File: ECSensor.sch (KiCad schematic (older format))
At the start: 11 parts, among them J4 EC_Sensor_Input_3_Pin, Q1 Q_PMOS_DSG

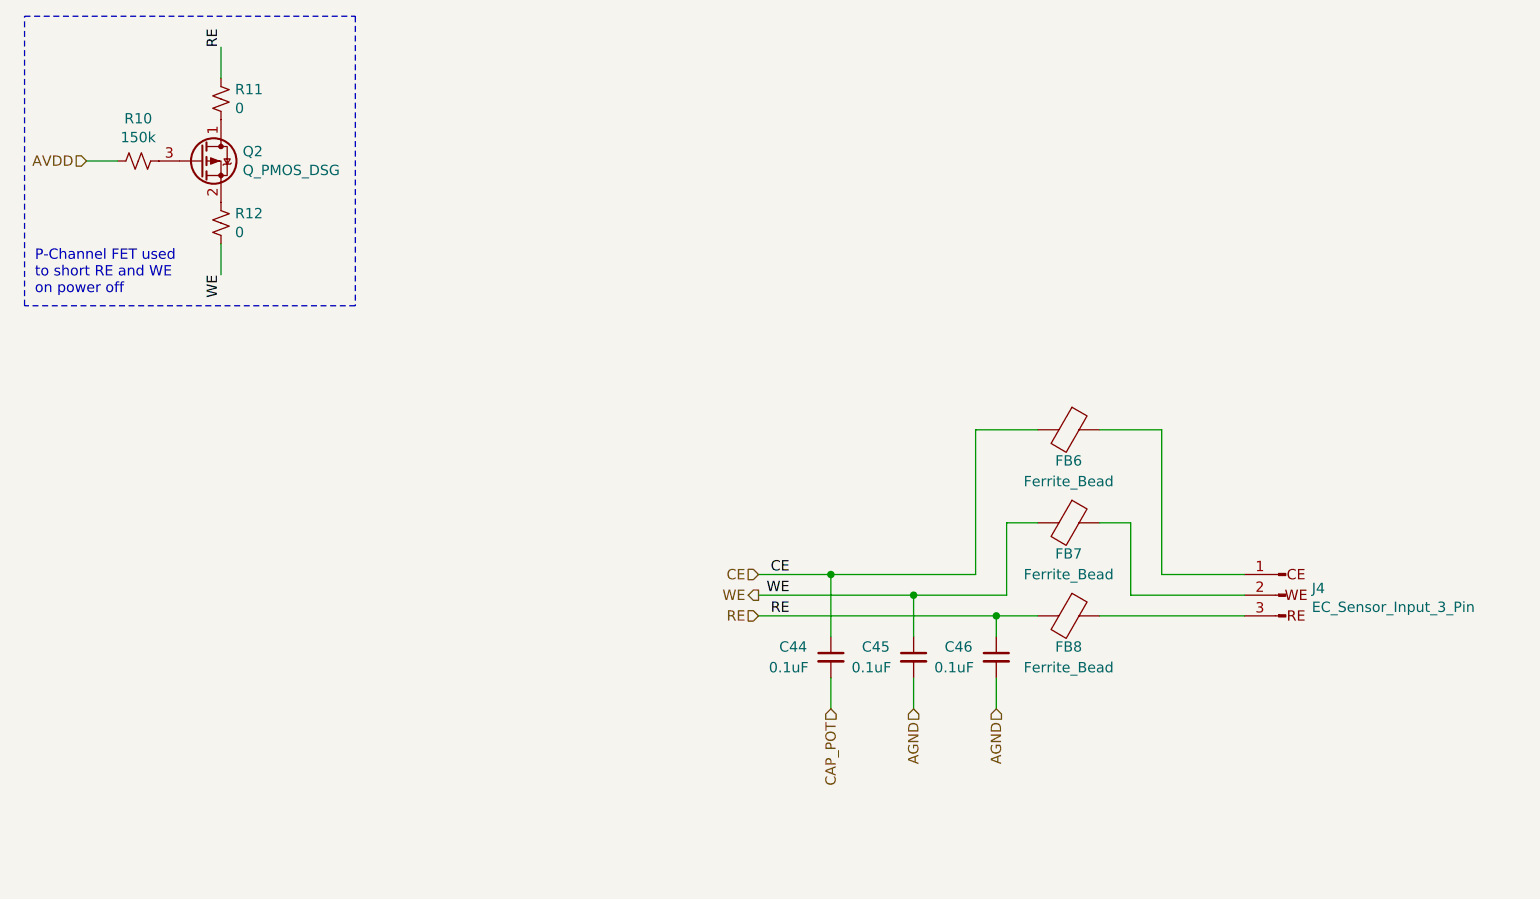
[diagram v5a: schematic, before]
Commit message: removed unneccary components to free up both channels
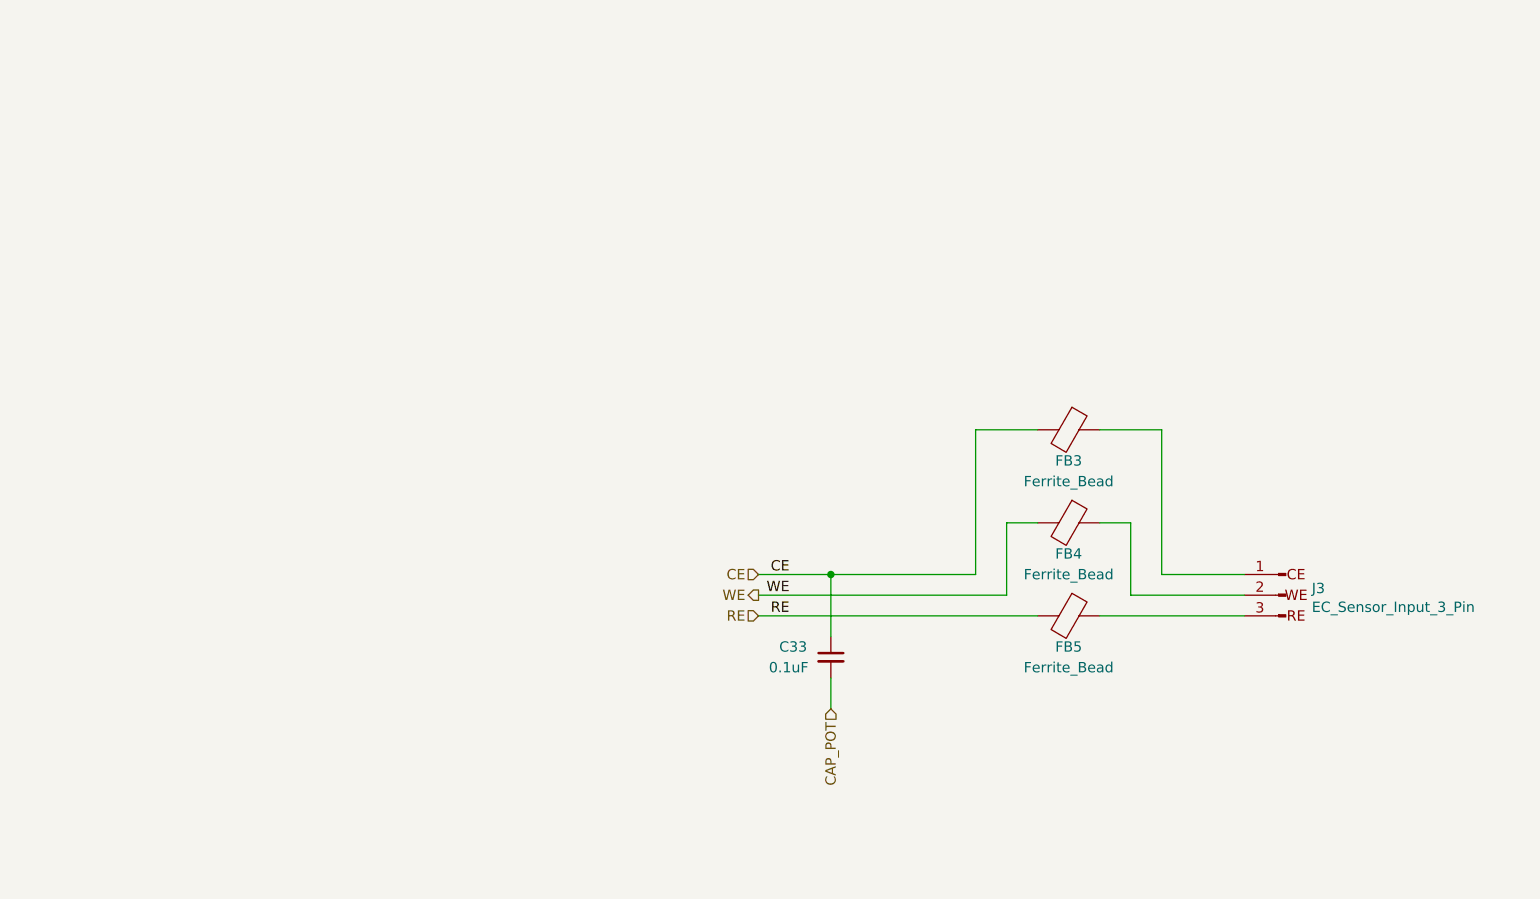
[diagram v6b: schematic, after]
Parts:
- removed C45, C46: 0.1uF, Capacitor_SMD:C_0402_1005Metric, symbol Device:C_Small
- removed Q1: Q_PMOS_DSG, Package_TO_SOT_SMD:SOT-23, symbol Device:Q_PMOS_DSG
- removed R7: 150k, Resistor_SMD:R_0402_1005Metric, symbol Device:R_Small_US
- removed R8, R9: 0, Resistor_SMD:R_0402_1005Metric, symbol Device:R_Small_US
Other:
- note removed: "P-Channel FET used \nto short RE and WE\non power off"
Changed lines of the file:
@@
 $Descr A4 11693 8268
 encoding utf-8
-Sheet 5 5
+Sheet 2 5
 Title "Potentiostat Frontend"
 Date "2021-02-10"
@@
 $EndDescr
 $Comp
-L Device:C_Small C45
-U 1 1 5DF76279
-P 5000 3750
-AR Path="/5DF7340A/5DF76279" Ref="C45"  Part="1"
-AR Path="/5DF54D0C/5DF76279" Ref="C34"  Part="1"
-F 0 "C45" H 4750 3800 50  0000 L CNN
-F 1 "0.1uF" H 4700 3700 50  0000 L CNN
-F 2 "Capacitor_SMD:C_0402_1005Metric" H 5000 3750 50  0001 C CNN
-F 3 "~" H 5000 3750 50  0001 C CNN
-	1    5000 3750
-	1    0    0    -1
-$EndComp
-$Comp
 L Device:C_Small C44
 U 1 1 5DF76497
@@
 AR Path="/5DF7340A/5DF76497" Ref="C44"  Part="1"
 AR Path="/5DF54D0C/5DF76497" Ref="C33"  Part="1"
-F 0 "C44" H 4350 3800 50  0000 L CNN
+F 0 "C33" H 4350 3800 50  0000 L CNN
 F 1 "0.1uF" H 4300 3700 50  0000 L CNN
 F 2 "Capacitor_SMD:C_0402_1005Metric" H 4600 3750 50  0001 C CNN
 F 3 "~" H 4600 3750 50  0001 C CNN
 	1    4600 3750
-	1    0    0    -1
-$EndComp
-$Comp
-L Device:C_Small C46
-U 1 1 5DF768A0
-P 5400 3750
-AR Path="/5DF7340A/5DF768A0" Ref="C46"  Part="1"
-AR Path="/5DF54D0C/5DF768A0" Ref="C35"  Part="1"
-F 0 "C46" H 5150 3800 50  0000 L CNN
-F 1 "0.1uF" H 5100 3700 50  0000 L CNN
-F 2 "Capacitor_SMD:C_0402_1005Metric" H 5400 3750 50  0001 C CNN
-F 3 "~" H 5400 3750 50  0001 C CNN
-	1    5400 3750
 	1    0    0    -1
 $EndComp
@@
 AR Path="/5DF7340A/5DF7EEA4" Ref="J4"  Part="1"
 AR Path="/5DF54D0C/5DF7EEA4" Ref="J3"  Part="1"
-F 0 "J4" H 6674 3483 50  0000 R CNN
+F 0 "J3" H 6674 3483 50  0000 R CNN
 F 1 "EC_Sensor_Input_3_Pin" H 6674 3392 50  0000 R CNN
 F 2 "Connector_PinHeader_2.54mm:PinHeader_1x03_P2.54mm_Horizontal" H 6800 3450 50  0001 C CNN
@@
 Text HLabel 4250 3350 0    50   Input ~ 0
 CE
-$Comp
-L Device:Q_PMOS_DSG Q1
-U 1 1 5E0080C3
-P 1550 1350
-AR Path="/5DF54D0C/5E0080C3" Ref="Q1"  Part="1"
-AR Path="/5DF7340A/5E0080C3" Ref="Q2"  Part="1"
-F 0 "Q2" H 1755 1396 50  0000 L CNN
-F 1 "Q_PMOS_DSG" H 1755 1305 50  0000 L CNN
-F 2 "Package_TO_SOT_SMD:SOT-23" H 1750 1450 50  0001 C CNN
-F 3 "~" H 1550 1350 50  0001 C CNN
-	1    1550 1350
-	1    0    0    -1
-$EndComp
-$Comp
-L Device:R_Small_US R7
-U 1 1 5E00BDC0
-P 1250 1350
-AR Path="/5DF54D0C/5E00BDC0" Ref="R7"  Part="1"
-AR Path="/5DF7340A/5E00BDC0" Ref="R10"  Part="1"
-F 0 "R10" V 1045 1350 50  0000 C CNN
-F 1 "150k" V 1136 1350 50  0000 C CNN
-F 2 "Resistor_SMD:R_0402_1005Metric" H 1250 1350 50  0001 C CNN
-F 3 "~" H 1250 1350 50  0001 C CNN
-	1    1250 1350
-	0    1    1    0
-$EndComp
-$Comp
-L Device:R_Small_US R8
-U 1 1 5E00C4B8
-P 1650 1050
-AR Path="/5DF54D0C/5E00C4B8" Ref="R8"  Part="1"
-AR Path="/5DF7340A/5E00C4B8" Ref="R11"  Part="1"
-F 0 "R11" H 1582 1004 50  0000 R CNN
-F 1 "0" H 1582 1095 50  0000 R CNN
-F 2 "Resistor_SMD:R_0402_1005Metric" H 1650 1050 50  0001 C CNN
-F 3 "~" H 1650 1050 50  0001 C CNN
-	1    1650 1050
-	-1   0    0    1
-$EndComp
-$Comp
-L Device:R_Small_US R9
-U 1 1 5E00C73E
-P 1650 1650
-AR Path="/5DF54D0C/5E00C73E" Ref="R9"  Part="1"
-AR Path="/5DF7340A/5E00C73E" Ref="R12"  Part="1"
-F 0 "R12" H 1718 1696 50  0000 L CNN
-F 1 "0" H 1718 1605 50  0000 L CNN
-F 2 "Resistor_SMD:R_0402_1005Metric" H 1650 1650 50  0001 C CNN
-F 3 "~" H 1650 1650 50  0001 C CNN
-	1    1650 1650
-	1    0    0    -1
-$EndComp
-Wire Wire Line
-	1000 1350 1150 1350
-Text Label 1650 800  1    50   ~ 0
-RE
-Text Label 1650 1900 3    50   ~ 0
-WE
-Wire Wire Line
-	1650 1750 1650 1900
-Wire Wire Line
-	1650 950  1650 800
-Wire Notes Line style solid
-	2300 650  2300 2050
-Wire Notes Line style solid
-	2300 2050 700  2050
-Wire Notes Line style solid
-	700  2050 700  650
-Wire Notes Line style solid
-	700  650  2300 650
-Text Notes 750  2000 0    50   ~ 0
-P-Channel FET used \nto short RE and WE\non power off
 Wire Wire Line
 	4600 4000 4600 3850
-Wire Wire Line
-	5400 3850 5400 4000
-Wire Wire Line
-	5000 4000 5000 3850
 Wire Wire Line
 	6600 3450 6050 3450
@@
 	5300 3350 4600 3350
 Wire Wire Line
-	5450 3450 5000 3450
-Wire Wire Line
 	4600 3650 4600 3350
 Connection ~ 4600 3350
-Wire Wire Line
-	5000 3650 5000 3450
-Connection ~ 5000 3450
-Wire Wire Line
-	5400 3650 5400 3550
 $Comp
 L Device:Ferrite_Bead FB6
@@
 AR Path="/5DF7340A/605069B7" Ref="FB6"  Part="1"
 AR Path="/5DF54D0C/605069B7" Ref="FB3"  Part="1"
-F 0 "FB6" V 5900 2650 50  0000 C CNN
+F 0 "FB3" V 5900 2650 50  0000 C CNN
 F 1 "Ferrite_Bead" V 6000 2650 50  0000 C CNN
 F 2 "Inductor_SMD:L_0402_1005Metric" V 5680 2650 50  0001 C CNN
@@
 AR Path="/5DF7340A/60542E8C" Ref="FB7"  Part="1"
 AR Path="/5DF54D0C/60542E8C" Ref="FB4"  Part="1"
-F 0 "FB7" V 5900 3100 50  0000 C CNN
+F 0 "FB4" V 5900 3100 50  0000 C CNN
 F 1 "Ferrite_Bead" V 6000 3100 50  0000 C CNN
 F 2 "Inductor_SMD:L_0402_1005Metric" V 5680 3100 50  0001 C CNN
@@
 AR Path="/5DF7340A/6054431B" Ref="FB8"  Part="1"
 AR Path="/5DF54D0C/6054431B" Ref="FB5"  Part="1"
-F 0 "FB8" V 5900 3550 50  0000 C CNN
+F 0 "FB5" V 5900 3550 50  0000 C CNN
 F 1 "Ferrite_Bead" V 6000 3550 50  0000 C CNN
 F 2 "Inductor_SMD:L_0402_1005Metric" V 5680 3550 50  0001 C CNN
@@
 	5600 3100 5450 3100
 Wire Wire Line
-	5600 3550 5400 3550
-Connection ~ 5400 3550
-Wire Wire Line
 	5900 3550 6600 3550
 Wire Wire Line
 	4250 3350 4600 3350
 Wire Wire Line
-	4250 3450 5000 3450
+	4250 3550 5600 3550
 Wire Wire Line
-	4250 3550 5400 3550
-Text HLabel 1000 1350 0    50   Input ~ 0
-AVDD
-Text HLabel 5000 4000 3    50   Input ~ 0
-AGND
-Text HLabel 5400 4000 3    50   Input ~ 0
-AGND
+	4250 3450 5450 3450
 $EndSCHEMATC
